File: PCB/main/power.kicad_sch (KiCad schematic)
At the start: 40 parts, among them IC1 TP4056-42-ESOP8, IC2 AMS1117-3.3, IC3 74HC04D,653, J5 MICROXNJ, M1 MPMOS, M2 MPMOS, M3 MNMOS, M4 MNMOS, Q1 Q_PNP_BCE, Q2 Q_PMOS_GDS, Q3 Q_PMOS_DGS, Q4 2N3904, Q5 Q_NMOS_DSG, U1 LM393, U2 LT1492

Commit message: Power v0.1, Sensing v0.1, uC Control v0.1, Simulations
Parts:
- removed D3, D5: D_Zener, symbol Device:D_Zener
- removed D4: White LED, symbol Device:LED
- removed IC3: 74HC04D,653, SOIC127P600X175-14N, symbol 74HC04D-653:74HC04D,653
- removed M1, M2: MPMOS, symbol pspice:MPMOS
- removed M3, M4: MNMOS, symbol pspice:MNMOS
- removed Q1: Q_PNP_BCE, symbol Device:Q_PNP_BCE
- removed Q2: Q_PMOS_GDS, symbol Device:Q_PMOS_GDS
- removed Q3: Q_PMOS_DGS, symbol Device:Q_PMOS_DGS
- removed Q4: 2N3904, Package_TO_SOT_THT:TO-92_Inline, symbol Transistor_BJT:2N3904
- removed Q5: Q_NMOS_DSG, symbol Device:Q_NMOS_DSG
- removed R14, R15, R16, R4: 1kΩ, symbol Device:R_Small_US
- removed R7, R9: 10kΩ, symbol Device:R_Small_US
- removed U2: LT1492, symbol Amplifier_Operational:LT1492
- added C2: 10uF, symbol Device:C_Small
- added C4, C6: 1u, symbol Device:C_Small
- added D1, D2, D3, D6, D7: 1N5819WS, Diode_THT:D_DO-41_SOD81_P10.16mm_Horizontal, symbol Diode:1N5819
- added Q1, Q2, Q3: AO3401A, Package_TO_SOT_SMD:SOT-23, symbol Transistor_FET:AO3401A
- added R2, R3: 0R, symbol Device:R_Small_US
- added R5: 4.7k, symbol Device:R_Small_US
- BT1: Populate (none) -> DNP
- C1: value 10uF -> 1u; JLC Part Number (none) -> C52923; Price (none) -> $0.0037
- C3: renamed from C2; JLC Part Number (none) -> C19702; Price (none) -> $0.068
- C5: renamed from C3; value C_Small -> 1u; JLC Part Number (none) -> C52923; Price (none) -> $0.0037
- D4: renamed from D1; JLC Part Number (none) -> C72043; Price (none) -> $0.0312
- D5: renamed from D2; JLC Part Number (none) -> C84256; Price (none) -> $0.0139
- IC1: JLC Part Number (none) -> C16581; Price (none) -> $0.2578
- IC2: JLC Part Number (none) -> C6186; Price (none) -> $0.1855
- J5: JLC Part Number (none) -> C404969; Price (none) -> $0.6496
- R1: value 0.4Ω -> 0R; JLC Part Number (none) -> C17477; Price (none) -> 0.0024
- R10: value 1kΩ -> 3.3k; JLC Part Number (none) -> C22978; Price (none) -> 0.0013
- R11: value 1kΩ -> 4.7k; JLC Part Number (none) -> C17673; Price (none) -> 0.0027
- R12: value 10kΩ -> 120kΩ; Field5 (none) -> $0.0007; JLC Part Number (none) -> C25750; Price (none) -> $0.0007
- R13: value 1kΩ -> 10k; JLC Part Number (none) -> C25744; Price (none) -> $0.0007
- R4: renamed from R2; value 10kΩ -> 100Ω; JLC Part Number (none) -> C17901; Price (none) -> $0.0043
- R6: value 10kΩ -> 4.7k; JLC Part Number (none) -> C17673; Price (none) -> 0.0027
- R7: renamed from R3; Field5 (none) -> $0.0007; JLC Part Number (none) -> C25905; Price (none) -> $0.0007
- R8: value 10kΩ -> 1kΩ; Field5 (none) -> $0.0007; JLC Part Number (none) -> C25905; Price (none) -> $0.0007
- R9: renamed from R5; value R -> 1k2; JLC Part Number (none) -> C22765; Price (none) -> $0.0014
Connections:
- net INVOUT is gone; now on an unnamed net: R1.1
- net VRegulated is gone; now on net +3V0: IC2.2 (VOUT)
- net BAT +: now also C4.1, Q2.3 (D); no longer R10.1, R11.1
- net D+: now also R2.1; no longer J5.3
- net D-: now also R3.1; no longer J5.2
- net GND: now also R11.1, R13.2, C2.2, C4.2, C6.2, D7.2 (A), Q2.1 (G), R5.2; no longer R8.2
- net POWEROUT: now also Q3.2 (S)
- net USBDETECT: now also R6.1; no longer R12.1
- net VCCBus: now also C1.1, D2.1 (K), Q1.3 (D); no longer J5.1
- net VPolarity: now also C5.1, IC2.3 (VIN), R1.2, D1.1 (K), D6.1 (K), Q1.2 (S); no longer R6.2, U1.3 (+)
- net at D5.1 (K): now also R8.1
- net at D4.2 (A), D5.2 (A), IC1.4 (VCC)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: now also C2.1; no longer C1.1, R1.2
- net at IC2.1 (GND/ADJ): now also R10.1, R11.2; no longer R8.1
- net at R4.1: now also D1.2 (A), Q1.1 (G)
- net at IC1.7 (~{CHRG}): now also R8.2
- net at R12.2: now also R13.1, U1.3 (+)
- net +3V0: now reaches R10.2
- net +3V0: now also U1.2 (-), C6.1, D6.2 (A)
- net at U1.1: now also Q3.1 (G)
- removed net 5VSupply: C5.1, IC2.3 (VIN), R6.1, U1.2 (-)
- new net: D2.2 (A), D3.2 (A), J5.1
- new net: J5.2, R3.2
- new net: J5.3, R2.2
- new net: D3.1 (K), R5.1, R6.2
- new net BATOUT: D7.1 (K), Q2.2 (S), Q3.3 (D), R12.1
- no-connect marks 12 -> 2
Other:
- note added: "Check IC can take in ~3.6V"
- note added: "Check IC can take in ~4V"
- note added: "Schottky Diode included for simulation. AO3401A includes one"
- note added: "USB Input & Detection"
- note added: "Under Voltage Cutout Protection"
- note removed: "AND Gate for Charging Logic"
- note removed: "Inverter for Charger"
- note removed: "Power from the USB when powering the HAT using laptop power instead of battery (Need a switch system)"
- note removed: "USB Detection"
- note removed: "USB Input"
- note removed: "Under Voltage Cutout Protection (Still need to update R values)"
- moved on the sheet: BT1, C3, C5, D4, D5, IC1, IC2, R4, R7, R9

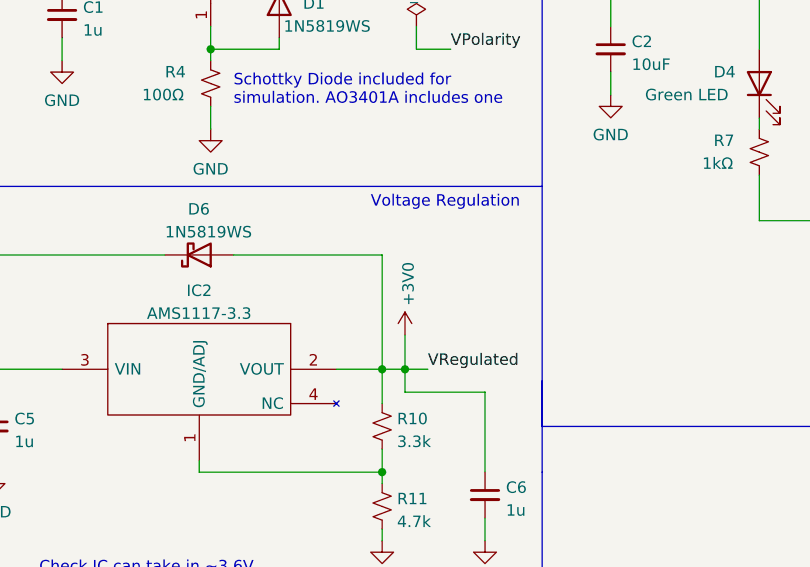
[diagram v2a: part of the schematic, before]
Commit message: Power v0.1, Sensing v0.1, uC Control v0.1, ERC
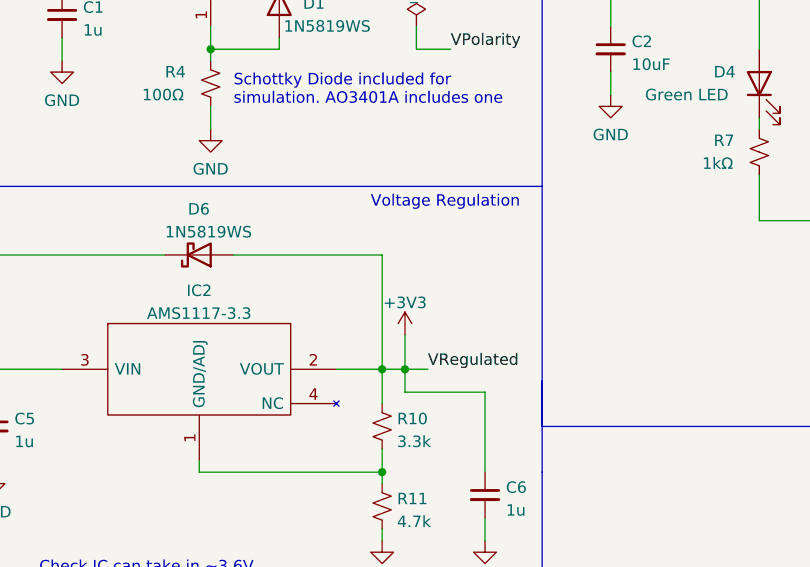
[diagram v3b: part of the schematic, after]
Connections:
- net +3V0 renamed +3V3
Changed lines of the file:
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@@
   (symbol (lib_id "power:GND") (at 223.52 154.94 0) (unit 1)
     (in_bom yes) (on_board yes) (fields_autoplaced)
-    (property "Reference" "#PWR033" (id 0) (at 223.52 161.29 0)
+    (property "Reference" "#PWR035" (id 0) (at 223.52 161.29 0)
       (effects (font (size 1.27 1.27)) hide)
     )
@@
     (pin "1")
   )
+  (symbol (lib_id "power:+3V3") (at 147.32 97.79 0) (unit 1)
+    (in_bom yes) (on_board yes) (fields_autoplaced)
+    (property "Reference" "#PWR027" (id 0) (at 147.32 101.6 0)
+      (effects (font (size 1.27 1.27)) hide)
+    )
+    (property "Value" "+3V3" (id 1) (at 147.32 94.2142 0))
+    (property "Footprint" "" (id 2) (at 147.32 97.79 0)
+      (effects (font (size 1.27 1.27)) hide)
+    )
+    (property "Datasheet" "" (id 3) (at 147.32 97.79 0)
+      (effects (font (size 1.27 1.27)) hide)
+    )
+    (pin "1")
+  )
   (symbol (lib_id "Device:R_Small_US") (at 144.78 107.95 180) (unit 1)
     (in_bom yes) (on_board yes) (fields_autoplaced)
@@
   (symbol (lib_id "power:GND") (at 248.92 100.33 0) (unit 1)
     (in_bom yes) (on_board yes)
-    (property "Reference" "#PWR028" (id 0) (at 248.92 106.68 0)
+    (property "Reference" "#PWR030" (id 0) (at 248.92 106.68 0)
       (effects (font (size 1.27 1.27)) hide)
     )
@@
   (symbol (lib_id "power:GND") (at 259.08 63.5 0) (unit 1)
     (in_bom yes) (on_board yes)
-    (property "Reference" "#PWR017" (id 0) (at 259.08 69.85 0)
+    (property "Reference" "#PWR019" (id 0) (at 259.08 69.85 0)
       (effects (font (size 1.27 1.27)) hide)
     )
@@
   (symbol (lib_id "power:GND") (at 156.21 120.65 0) (unit 1)
     (in_bom yes) (on_board yes) (fields_autoplaced)
-    (property "Reference" "#PWR032" (id 0) (at 156.21 127 0)
+    (property "Reference" "#PWR034" (id 0) (at 156.21 127 0)
       (effects (font (size 1.27 1.27)) hide)
     )
@@
   (symbol (lib_id "power:GND") (at 26.67 109.22 0) (unit 1)
     (in_bom yes) (on_board yes) (fields_autoplaced)
-    (property "Reference" "#PWR029" (id 0) (at 26.67 115.57 0)
+    (property "Reference" "#PWR031" (id 0) (at 26.67 115.57 0)
       (effects (font (size 1.27 1.27)) hide)
     )
@@
   (symbol (lib_id "power:GND") (at 257.81 88.9 0) (unit 1)
     (in_bom yes) (on_board yes) (fields_autoplaced)
-    (property "Reference" "#PWR024" (id 0) (at 257.81 95.25 0)
+    (property "Reference" "#PWR026" (id 0) (at 257.81 95.25 0)
       (effects (font (size 1.27 1.27)) hide)
     )
@@
   (symbol (lib_id "power:GND") (at 46.99 72.39 0) (mirror y) (unit 1)
     (in_bom yes) (on_board yes) (fields_autoplaced)
-    (property "Reference" "#PWR021" (id 0) (at 46.99 78.74 0)
+    (property "Reference" "#PWR023" (id 0) (at 46.99 78.74 0)
       (effects (font (size 1.27 1.27)) hide)
     )
@@
   (symbol (lib_id "power:GND") (at 241.3 100.33 0) (unit 1)
     (in_bom yes) (on_board yes)
-    (property "Reference" "#PWR027" (id 0) (at 241.3 106.68 0)
+    (property "Reference" "#PWR029" (id 0) (at 241.3 106.68 0)
       (effects (font (size 1.27 1.27)) hide)
     )
@@
   (symbol (lib_id "power:GND") (at 101.6 113.03 0) (unit 1)
     (in_bom yes) (on_board yes) (fields_autoplaced)
-    (property "Reference" "#PWR030" (id 0) (at 101.6 119.38 0)
+    (property "Reference" "#PWR032" (id 0) (at 101.6 119.38 0)
       (effects (font (size 1.27 1.27)) hide)
     )
@@
   (symbol (lib_id "power:GND") (at 125.73 74.93 0) (unit 1)
     (in_bom yes) (on_board yes) (fields_autoplaced)
-    (property "Reference" "#PWR023" (id 0) (at 125.73 81.28 0)
+    (property "Reference" "#PWR025" (id 0) (at 125.73 81.28 0)
       (effects (font (size 1.27 1.27)) hide)
     )
@@
   (symbol (lib_id "power:GND") (at 90.17 73.66 0) (mirror y) (unit 1)
     (in_bom yes) (on_board yes) (fields_autoplaced)
-    (property "Reference" "#PWR022" (id 0) (at 90.17 80.01 0)
+    (property "Reference" "#PWR024" (id 0) (at 90.17 80.01 0)
       (effects (font (size 1.27 1.27)) hide)
     )
@@
     (pin "2")
   )
-  (symbol (lib_id "power:+3V0") (at 147.32 97.79 0) (unit 1)
-    (in_bom yes) (on_board yes)
-    (property "Reference" "#PWR025" (id 0) (at 147.32 101.6 0)
-      (effects (font (size 1.27 1.27)) hide)
-    )
-    (property "Value" "+3V0" (id 1) (at 147.701 94.5388 90)
-      (effects (font (size 1.27 1.27)) (justify left))
-    )
-    (property "Footprint" "" (id 2) (at 147.32 97.79 0)
-      (effects (font (size 1.27 1.27)) hide)
-    )
-    (property "Datasheet" "" (id 3) (at 147.32 97.79 0)
-      (effects (font (size 1.27 1.27)) hide)
-    )
-    (pin "1")
-  )
   (symbol (lib_id "power:GND") (at 223.52 100.33 0) (unit 1)
     (in_bom yes) (on_board yes)
-    (property "Reference" "#PWR026" (id 0) (at 223.52 106.68 0)
+    (property "Reference" "#PWR028" (id 0) (at 223.52 106.68 0)
       (effects (font (size 1.27 1.27)) hide)
     )
@@
   (symbol (lib_id "power:GND") (at 170.18 71.12 0) (unit 1)
     (in_bom yes) (on_board yes) (fields_autoplaced)
-    (property "Reference" "#PWR020" (id 0) (at 170.18 77.47 0)
+    (property "Reference" "#PWR022" (id 0) (at 170.18 77.47 0)
       (effects (font (size 1.27 1.27)) hide)
     )
@@
   (symbol (lib_id "power:GND") (at 144.78 120.65 0) (unit 1)
     (in_bom yes) (on_board yes)
-    (property "Reference" "#PWR031" (id 0) (at 144.78 127 0)
+    (property "Reference" "#PWR033" (id 0) (at 144.78 127 0)
       (effects (font (size 1.27 1.27)) hide)
     )
@@
   (symbol (lib_id "power:GND") (at 15.24 69.85 0) (mirror y) (unit 1)
     (in_bom yes) (on_board yes) (fields_autoplaced)
-    (property "Reference" "#PWR019" (id 0) (at 15.24 76.2 0)
+    (property "Reference" "#PWR021" (id 0) (at 15.24 76.2 0)
       (effects (font (size 1.27 1.27)) hide)
     )
@@
   (symbol (lib_id "power:GND") (at 109.22 67.31 0) (unit 1)
     (in_bom yes) (on_board yes) (fields_autoplaced)
-    (property "Reference" "#PWR018" (id 0) (at 109.22 73.66 0)
-      (effects (font (size 1.27 1.27)) hide)
-    )
+    (property "Reference" "#PWR020" (id 0) (at 109.22 73.66 0)
+      (effects (font (size 1.27 1.27)) hide)
+    )

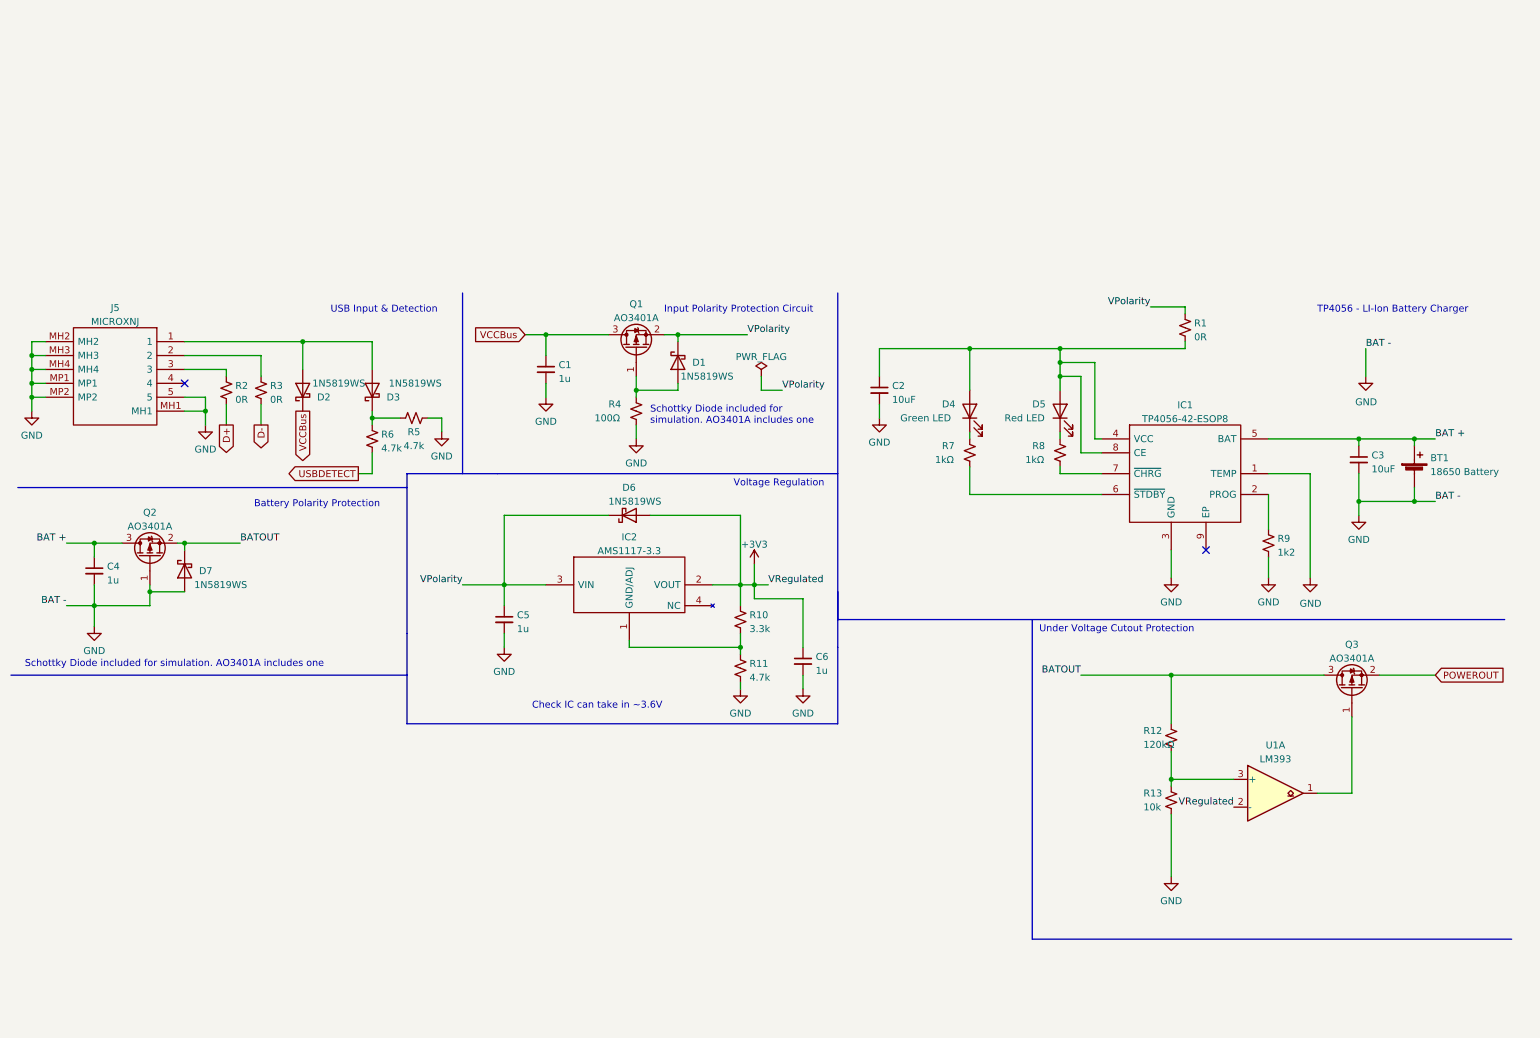
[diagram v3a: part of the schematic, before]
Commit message: Schematic updates
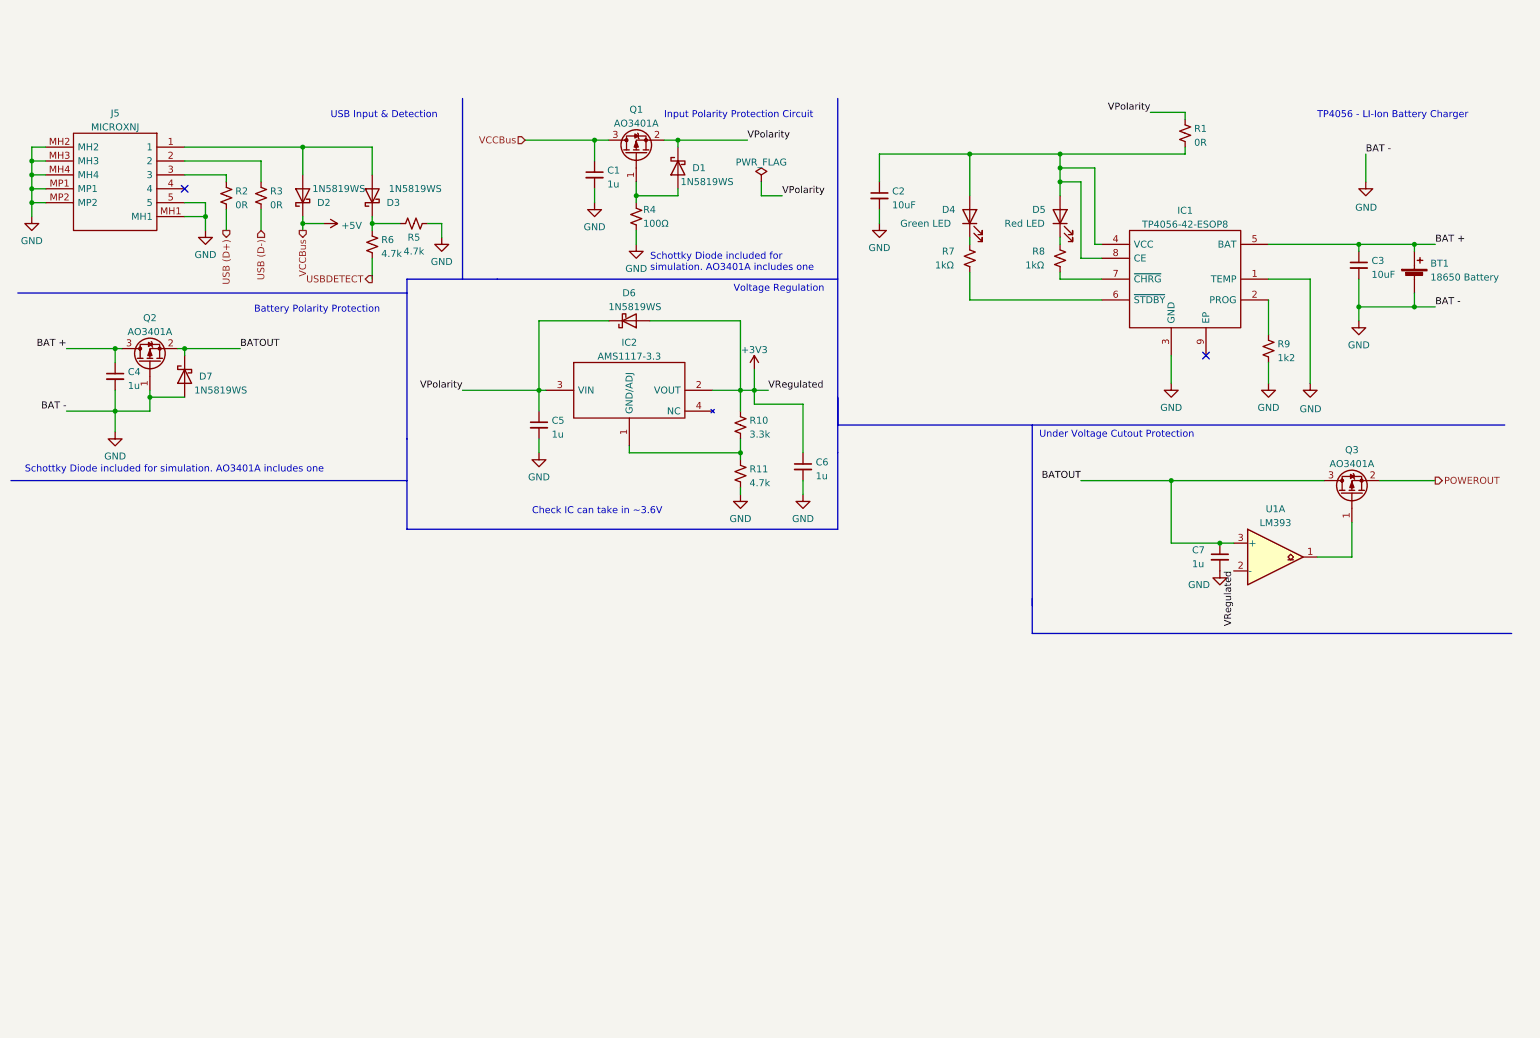
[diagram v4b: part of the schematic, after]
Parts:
- removed R12: 120kΩ, symbol Device:R_Small_US
- removed R13: 10k, symbol Device:R_Small_US
- added C7: 1u, symbol Device:C_Small
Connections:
- net BATOUT: now also U1.3 (+), C7.1
- net GND: now also C7.2
- net D+ renamed USB (D+)
- net D- renamed USB (D-)
- net VCCBus renamed +5V
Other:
- moved on the sheet: BT1, C1, C2, C3, C4, C5, C6, D1, D2, D3, D4, D5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

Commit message: Power, uC, Sensing v0.1.1
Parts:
- removed D1, D7: 1N5819WS, Diode_THT:D_DO-41_SOD81_P10.16mm_Horizontal, symbol Diode:1N5819
- added R10, R12, R15, R2: 0R, 0R:RESC2013X65N, symbol Device:R_Small_US
- added TP1, TP2, TP3, TP4, TP5, TP6, TP7: TestPoint, TestPoint:TestPoint_Pad_D2.0mm, symbol Connector:TestPoint
- BT1: footprint (none) -> Battery:BatteryHolder_Keystone_1042_1x18650
- C1, C4, C5, C6, C7: footprint (none) -> 1uF_0804:CAPC1608X90N
- C2, C3: footprint (none) -> 10uF_0804:CAPC2012X145N
- D1: renamed from D2; footprint Diode_THT:D_DO-41_SOD81_P10.16mm_Horizontal -> Diode_SMD:D_SOD-323
- D2: renamed from D3; footprint Diode_THT:D_DO-41_SOD81_P10.16mm_Horizontal -> Diode_SMD:D_SOD-323
- D3: renamed from D4; footprint (none) -> Green_LED:LEDC1608X50N
- D4: renamed from D5; footprint (none) -> Red_LED:LEDC1608X70N
- IC1: footprint SOIC127P600X175-9N -> TP4506:SOIC127P600X175-9N
- IC2: footprint SOT229P700X180-4N -> AMS1117-3.3V:SOT229P700X180-4N
- J5: footprint MICROXNJ -> MICROXNJ:MICROXNJ
- Q1, Q2, Q3: footprint Package_TO_SOT_SMD:SOT-23 -> AO3401A:SOT95P280X125-3N
- R1: footprint (none) -> 0R:RESC2013X65N
- R11: renamed from R9; footprint (none) -> 1k:RESC1608X55N
- R13: renamed from R10; footprint (none) -> 3k3:RESC1608X55N
- R14: renamed from R11; footprint (none) -> 4k7:RESC2013X65N
- R3: renamed from R2; footprint (none) -> 0R:RESC2013X65N
- R4: renamed from R3; footprint (none) -> 0R:RESC2013X65N
- R5: renamed from R4; footprint (none) -> 100_ohm:RESC3116X65N
- R6: renamed from R5; footprint (none) -> 4k7:RESC2013X65N
- R7: renamed from R6; footprint (none) -> 4k7:RESC2013X65N
- R8: renamed from R7; footprint (none) -> 1k:RESC1608X55N
- R9: renamed from R8; footprint (none) -> 1k:RESC1608X55N
- U1: footprint (none) -> LMS393DRG:SOIC127P600X175-8N
- renumbered D6 to D5
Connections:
- net +3V3: no longer U1.2 (-)
- net BAT +: now also R10.2; no longer C4.1, Q2.3 (D)
- net BATOUT: now also R15.2, TP6.1; no longer C7.1, Q3.3 (D), U1.3 (+)
- net GND: now also Q3.1 (G), U1.1
- net USB (D+): now also TP3.1
- net USB (D-): now also TP4.1
- net USBDETECT: now also TP2.1
- net VPolarity: now also TP5.1; no longer C5.1, D5.1 (K), IC2.3 (VIN)
- net +5V: no longer names the net of C1.1, Q1.3 (D)
- net +5V: now also R2.1; no longer D1.1 (K)
- net POWEROUT renamed UVLO_OUT
- net UVLO_OUT: now also R12.2, TP7.1
- new net: C5.1, D5.1 (K), IC2.3 (VIN), R12.1
- new net: C7.1, Q3.3 (D), R15.1, U1.3 (+)
- new net: C4.1, Q2.3 (D), R10.1
- new net VCCBus: D1.1 (K), R2.2, TP1.1
- new net VRegulated: U1.2 (-)
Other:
- note removed: "Check IC can take in ~3.6V"
